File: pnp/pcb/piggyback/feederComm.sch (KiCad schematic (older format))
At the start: 60 parts, among them J10 F06, J11 F07, J12 F08, J13 F09, J14 F10, J15 F11, J16 F12, J17 F13, J18 F14, J19 F15, J20 F16, J21 F17, J22 F18, J23 F19, J24 F20, J25 F25, J26 F26, J27 F27, J28 F28, J29 F21, J30 F22, J31 F23, J32 F24, J33 F29, J34 F30, J35 F31, J36 F32, J5 F01, J6 F02, J7 F03, J8 F04, J9 F05, U1 MCP23017_SO_2, U3 MCP23017_SO_3, U4 MCP23017_SO_1, U5 MCP23017_SO_4

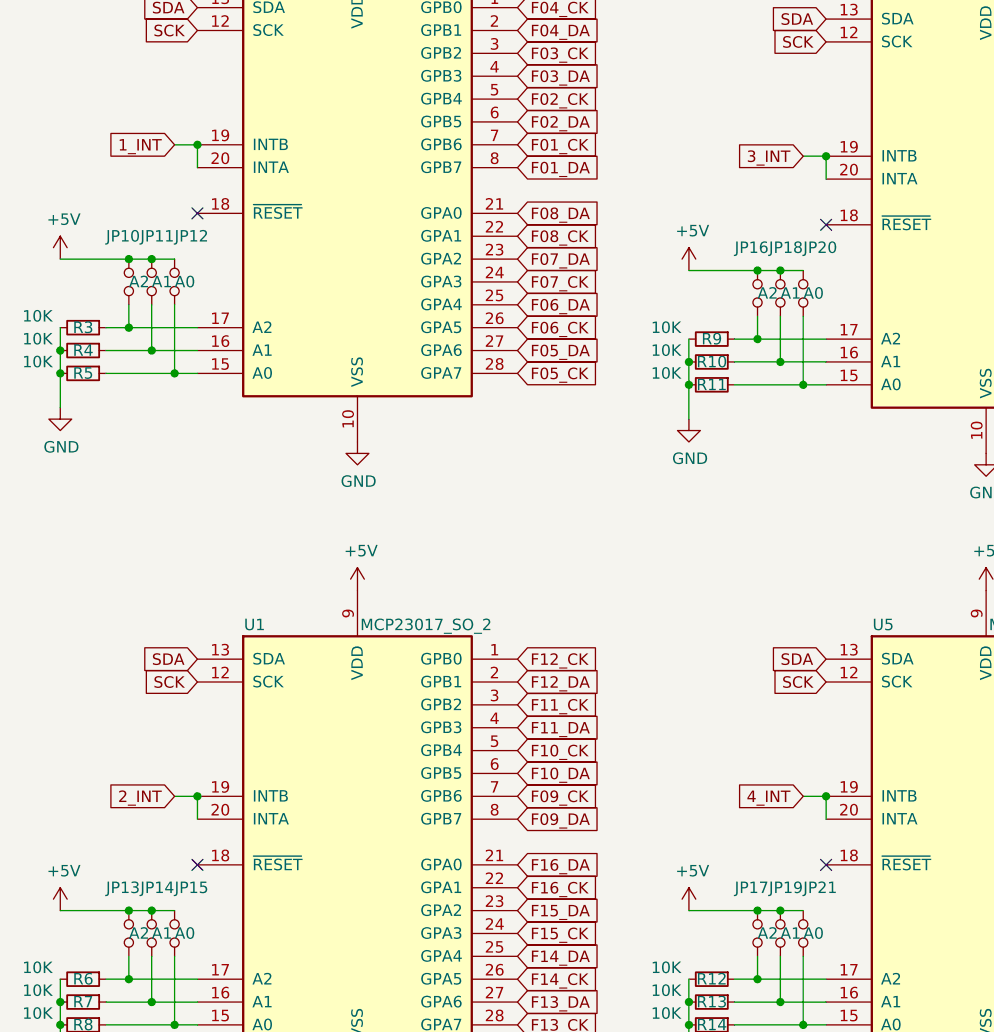
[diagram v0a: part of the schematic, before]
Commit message: Adding feeder and pnp CAD, updating Piggyback to fix USB, MCP23017 Reset pullup, and add uC reset button.
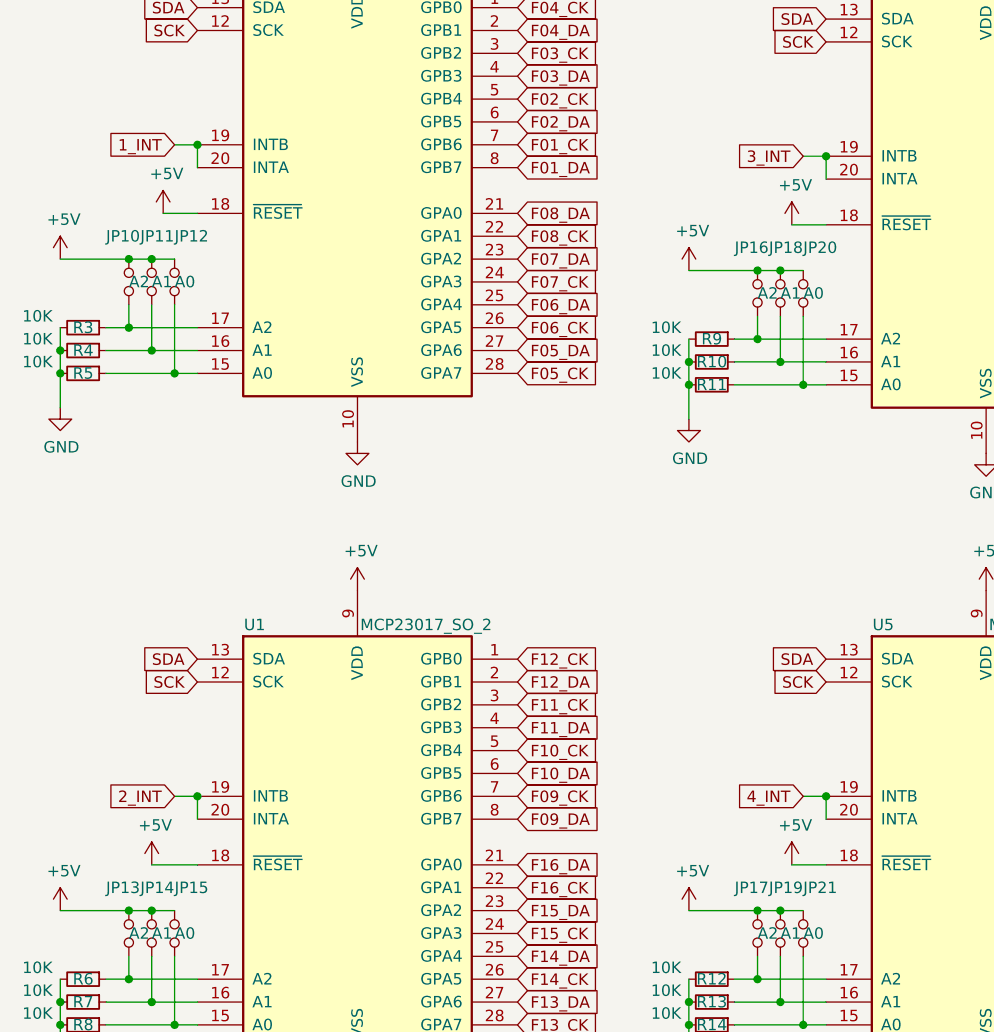
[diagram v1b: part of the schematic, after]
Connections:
- net +5V: now also U1.18 (~RESET~), U3.18 (~RESET~), U4.18 (~RESET~), U5.18 (~RESET~)
- no-connect marks 4 -> 0
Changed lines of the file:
@@
 	1400 2100 1400 2000
 Connection ~ 1400 2000
-NoConn ~ 4150 2350
-NoConn ~ 1400 2300
-NoConn ~ 1400 5150
-NoConn ~ 4150 5150
+$Comp
+L power:+5V #PWR0215
+U 1 1 5EA27907
+P 1250 2300
+F 0 "#PWR0215" H 1250 2150 50  0001 C CNN
+F 1 "+5V" H 1265 2473 50  0000 C CNN
+F 2 "" H 1250 2300 50  0001 C CNN
+F 3 "" H 1250 2300 50  0001 C CNN
+	1    1250 2300
+	1    0    0    -1
+$EndComp
+Wire Wire Line
+	1250 2300 1400 2300
+$Comp
+L power:+5V #PWR0216
+U 1 1 5EA3D5F8
+P 4000 2350
+F 0 "#PWR0216" H 4000 2200 50  0001 C CNN
+F 1 "+5V" H 4015 2523 50  0000 C CNN
+F 2 "" H 4000 2350 50  0001 C CNN
+F 3 "" H 4000 2350 50  0001 C CNN
+	1    4000 2350
+	1    0    0    -1
+$EndComp
+Wire Wire Line
+	4000 2350 4150 2350
+$Comp
+L power:+5V #PWR0217
+U 1 1 5EA43ABE
+P 4000 5150
+F 0 "#PWR0217" H 4000 5000 50  0001 C CNN
+F 1 "+5V" H 4015 5323 50  0000 C CNN
+F 2 "" H 4000 5150 50  0001 C CNN
+F 3 "" H 4000 5150 50  0001 C CNN
+	1    4000 5150
+	1    0    0    -1
+$EndComp
+Wire Wire Line
+	4000 5150 4150 5150
+$Comp
+L power:+5V #PWR0218
+U 1 1 5EA556DB
+P 1200 5150
+F 0 "#PWR0218" H 1200 5000 50  0001 C CNN
+F 1 "+5V" H 1215 5323 50  0000 C CNN
+F 2 "" H 1200 5150 50  0001 C CNN
+F 3 "" H 1200 5150 50  0001 C CNN
+	1    1200 5150
+	1    0    0    -1
+$EndComp
+Wire Wire Line
+	1200 5150 1400 5150
 $EndSCHEMATC
